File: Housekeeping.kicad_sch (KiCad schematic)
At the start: 117 parts, among them J5 PPS IN, J6 WP Jumper, Q1 FDN335N, Q2 FDN335N, U123 MAX4896, U15 AT24C64D-SSHM, U16 SI5330B-B00206-GM, U19 74AVC4T245, U36 TL071H, U37 TXU0101

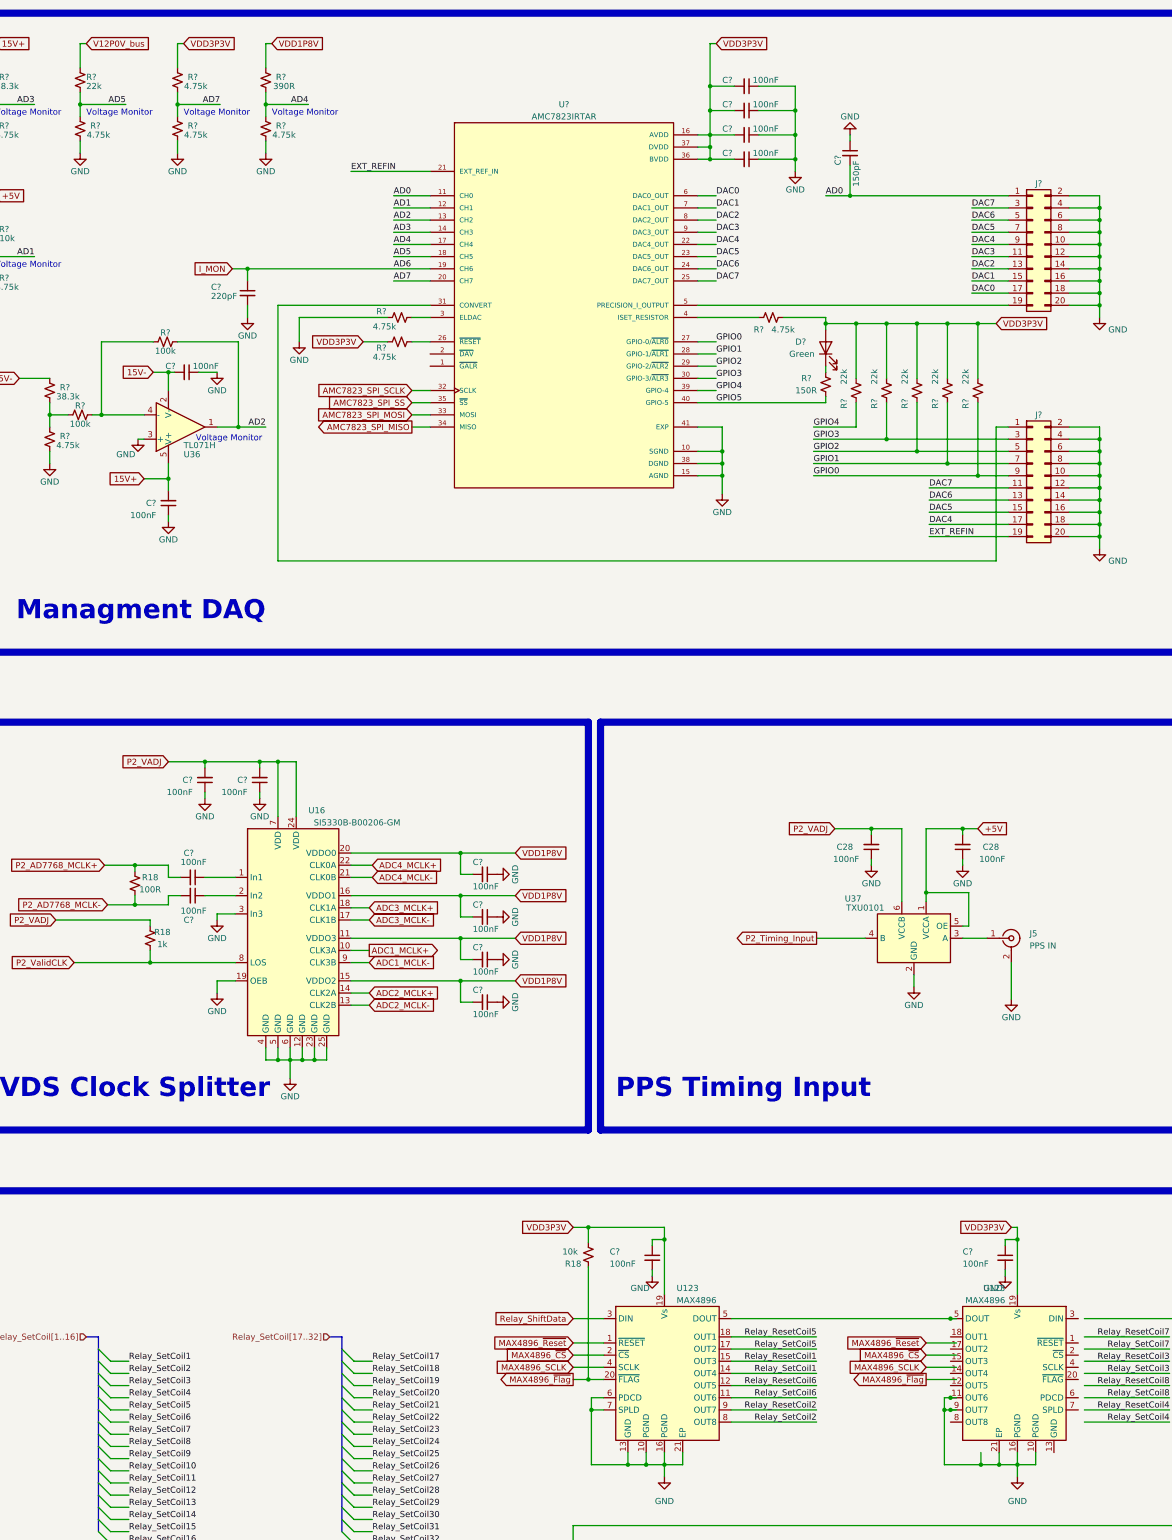
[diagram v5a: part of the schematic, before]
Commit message: Push Version before ADC change from 1.8V to 2.5V I/O
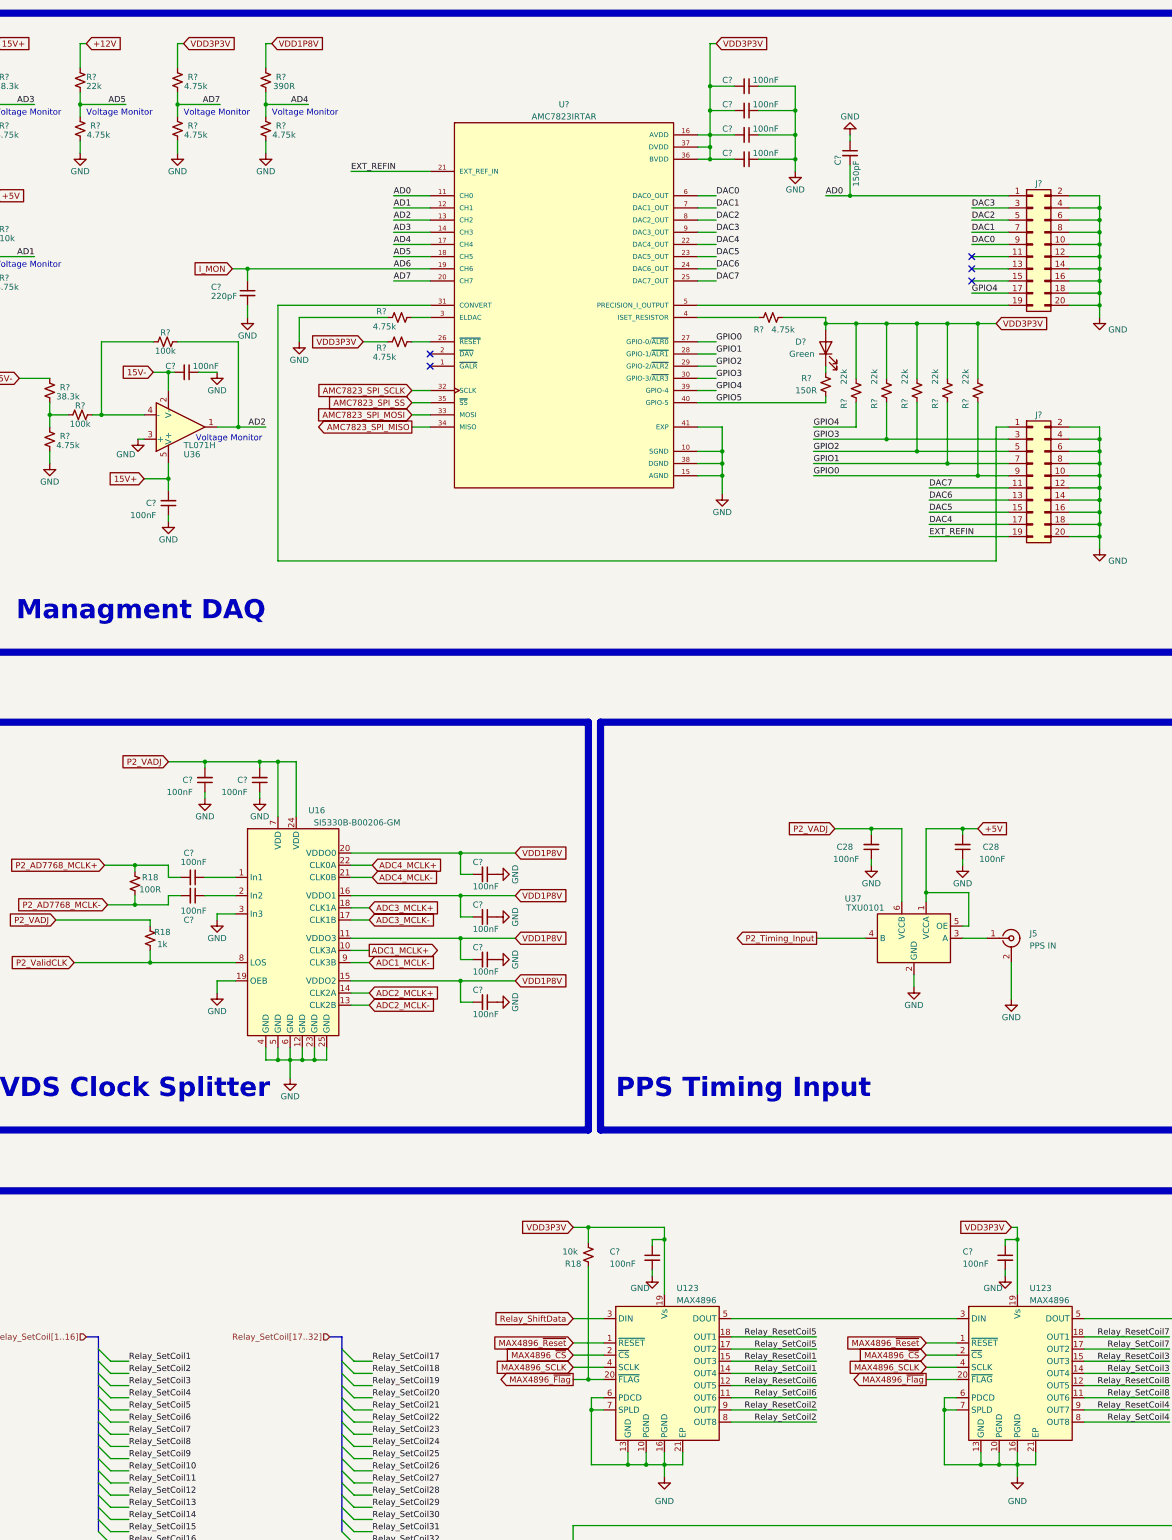
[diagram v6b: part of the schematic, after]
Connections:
- net DAC0: now also J?.9 (Pin_9); no longer J?.17 (Pin_17)
- net DAC1: now also J?.7 (Pin_7); no longer J?.15 (Pin_15)
- net DAC2: now also J?.5 (Pin_5); no longer J?.13 (Pin_13)
- net DAC3: now also J?.3 (Pin_3); no longer J?.11 (Pin_11)
- net DAC4: no longer J?.9 (Pin_9)
- net DAC5: no longer J?.7 (Pin_7)
- net DAC6: no longer J?.5 (Pin_5)
- net DAC7: no longer J?.3 (Pin_3)
- net GND: now also U123.13 (GND), U123.6 (PDCD), U123.7 (SPLD); no longer U123.11 (OUT6), U123.9 (OUT7)
- net GPIO4: now also J?.17 (Pin_17)
- net MAX4896_SCLK: now also U123.4 (SCLK)
- net MAX4896_~{CS}: now also U123.2 (~{CS})
- net MAX4896_~{Flag}: now also U123.20 (~{FLAG})
- net MAX4896_~{Reset}: now also U123.1 (~{RESET})
- net Relay_ResetCoil3: now also U123.15 (OUT3)
- net Relay_ResetCoil4: now also U123.9 (OUT7)
- net Relay_ResetCoil7: now also U123.18 (OUT1)
- net Relay_ResetCoil8: now also U123.12 (OUT5)
- net Relay_SetCoil3: now also U123.14 (OUT4)
- net Relay_SetCoil4: now also U123.8 (OUT8)
- net Relay_SetCoil7: now also U123.17 (OUT2)
- net Relay_SetCoil8: now also U123.11 (OUT6)
- net at U123.5 (DOUT): now also U123.3 (DIN); no longer U123.5 (DOUT)
- net at U123.3 (DIN): now also U123.5 (DOUT)
- net V12P0V_bus renamed +12V
- no-connect marks 1 -> 6
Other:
- moved on the sheet: U123
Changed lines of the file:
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@@
   (junction (at 452.12 154.94) (diameter 0) (color 0 0 0 0)
   )
-  (junction (at 221.615 307.34) (diameter 0) (color 0 0 0 0)
-  )
   (junction (at 252.73 66.675) (diameter 0) (color 0 0 0 0)
   )
-  (junction (at 221.615 288.29) (diameter 0) (color 0 0 0 0)
-  )
   (junction (at 78.74 34.925) (diameter 0) (color 0 0 0 0)
   )
@@
   (junction (at 252.73 74.295) (diameter 0) (color 0 0 0 0)
   )
-  (junction (at 221.615 304.8) (diameter 0) (color 0 0 0 0)
-  )
   (junction (at 408.94 120.015) (diameter 0) (color 0 0 0 0)
   )
@@
   (junction (at 220.98 109.855) (diameter 0) (color 0 0 0 0)
   )
+  (no_connect (at 113.03 89.535))
+  (no_connect (at 226.06 66.675))
+  (no_connect (at 226.06 71.755))
   (no_connect (at 539.75 67.945))
+  (no_connect (at 226.06 69.215))
+  (no_connect (at 113.03 86.995))
   (bus_entry (at 94.615 364.49) (size 2.54 2.54)
     (stroke (width 0) (type default))
@@
     (stroke (width 0) (type default))
   )
-  (wire (pts (xy 226.06 61.595) (xy 233.68 61.595))
-    (stroke (width 0) (type default))
-  )
   (wire (pts (xy 119.38 208.915) (xy 119.38 213.36))
     (stroke (width 0) (type default))
@@
     (stroke (width 0) (type default))
   )
-  (wire (pts (xy 175.895 288.29) (xy 221.615 288.29))
+  (wire (pts (xy 175.895 288.29) (xy 222.885 288.29))
     (stroke (width 0) (type default))
   )
@@
     (stroke (width 0) (type default))
   )
-  (wire (pts (xy 226.06 64.135) (xy 233.68 64.135))
-    (stroke (width 0) (type default))
-  )
   (wire (pts (xy 499.11 88.265) (xy 514.35 88.265))
     (stroke (width 0) (type default))
@@
     (stroke (width 0) (type default))
   )
-  (wire (pts (xy 222.885 307.34) (xy 221.615 307.34))
-    (stroke (width 0) (type default))
-  )
   (wire (pts (xy 227.965 387.35) (xy 231.775 387.35))
     (stroke (width 0) (type default))
@@
     (stroke (width 0) (type default))
   )
+  (bus (pts (xy 43.815 292.1) (xy 43.815 294.64))
+    (stroke (width 0) (type default))
+  )
   (wire (pts (xy 146.05 269.24) (xy 142.875 269.24))
     (stroke (width 0) (type default))
   )
+  (wire (pts (xy 226.06 64.135) (xy 233.68 64.135))
+    (stroke (width 0) (type default))
+  )
   (wire (pts (xy 323.215 370.84) (xy 340.995 370.84))
     (stroke (width 0) (type default))
@@
     (stroke (width 0) (type default))
   )
-  (bus (pts (xy 43.815 292.1) (xy 43.815 294.64))
-    (stroke (width 0) (type default))
-  )
   (wire (pts (xy 515.62 253.365) (xy 515.62 264.795))
     (stroke (width 0) (type default))
@@
     (stroke (width 0) (type default))
   )
-  (wire (pts (xy 222.885 304.8) (xy 221.615 304.8))
-    (stroke (width 0) (type default))
-  )
   (wire (pts (xy 226.06 71.755) (xy 233.68 71.755))
     (stroke (width 0) (type default))
@@
     (stroke (width 0) (type default))
   )
-  (wire (pts (xy 221.615 288.29) (xy 222.885 288.29))
-    (stroke (width 0) (type default))
-  )
   (wire (pts (xy 363.855 300.99) (xy 370.205 300.99))
     (stroke (width 0) (type default))
@@
     (stroke (width 0) (type default))
   )
+  (wire (pts (xy 226.06 61.595) (xy 233.68 61.595))
+    (stroke (width 0) (type default))
+  )
   (wire (pts (xy 46.355 349.25) (xy 50.165 349.25))
     (stroke (width 0) (type default))
@@
     (stroke (width 0) (type default))
   )
-  (wire (pts (xy 221.615 304.8) (xy 220.345 304.8))
+  (wire (pts (xy 220.345 304.8) (xy 222.885 304.8))
     (stroke (width 0) (type default))
   )
@@
     (stroke (width 0) (type default))
   )
+  (wire (pts (xy 226.06 59.055) (xy 233.68 59.055))
+    (stroke (width 0) (type default))
+  )
   (wire (pts (xy 325.755 102.235) (xy 329.565 102.235))
     (stroke (width 0) (type default))
@@
     (stroke (width 0) (type default))
   )
-  (wire (pts (xy 226.06 56.515) (xy 233.68 56.515))
-    (stroke (width 0) (type default))
-  )
   (wire (pts (xy 235.585 337.82) (xy 234.315 337.82))
     (stroke (width 0) (type default))
@@
     (stroke (width 0) (type default))
   )
-  (wire (pts (xy 226.06 59.055) (xy 233.68 59.055))
-    (stroke (width 0) (type default))
-  )
   (bus (pts (xy 43.815 344.17) (xy 43.815 346.71))
     (stroke (width 0) (type default))
@@
     (stroke (width 0) (type default))
   )
+  (wire (pts (xy 226.06 56.515) (xy 233.68 56.515))
+    (stroke (width 0) (type default))
+  )
   (wire (pts (xy 306.705 273.05) (xy 306.705 271.78))
     (stroke (width 0) (type default))
@@
     (stroke (width 0) (type default))
   )
-  (wire (pts (xy 221.615 307.34) (xy 220.345 307.34))
+  (wire (pts (xy 220.345 307.34) (xy 222.885 307.34))
     (stroke (width 0) (type default))
   )
@@
     (effects (font (size 1.27 1.27)) (justify left bottom))
   )
-  (label "DAC1" (at 226.06 71.755 0) (fields_autoplaced)
-    (effects (font (size 1.27 1.27)) (justify left bottom))
-  )
   (label "Relay_SetCoil2" (at 50.165 299.72 0) (fields_autoplaced)
     (effects (font (size 1.27 1.27)) (justify left bottom))
@@
     (effects (font (size 1.27 1.27)) (justify right bottom))
   )
-  (label "Relay_ResetCoil16" (at 50.165 379.73 0) (fields_autoplaced)
+  (label "DAC1" (at 226.06 61.595 0) (fields_autoplaced)
     (effects (font (size 1.27 1.27)) (justify left bottom))
   )
-  (label "DAC3" (at 226.06 66.675 0) (fields_autoplaced)
+  (label "Relay_ResetCoil16" (at 50.165 379.73 0) (fields_autoplaced)
     (effects (font (size 1.27 1.27)) (justify left bottom))
   )
@@
     (effects (font (size 1.27 1.27)) (justify left bottom))
   )
-  (label "DAC4" (at 226.06 64.135 0) (fields_autoplaced)
-    (effects (font (size 1.27 1.27)) (justify left bottom))
-  )
   (label "DAC6" (at 172.72 69.215 0) (fields_autoplaced)
     (effects (font (size 1.27 1.27)) (justify left bottom))
@@
     (effects (font (size 1.27 1.27)) (justify left bottom))
   )
+  (label "DAC3" (at 226.06 56.515 0) (fields_autoplaced)
+    (effects (font (size 1.27 1.27)) (justify left bottom))
+  )
   (label "Relay_ResetCoil10" (at 50.165 364.49 0) (fields_autoplaced)
     (effects (font (size 1.27 1.27)) (justify left bottom))
@@
     (effects (font (size 1.27 1.27)) (justify right bottom))
   )
-  (label "DAC6" (at 226.06 59.055 0) (fields_autoplaced)
-    (effects (font (size 1.27 1.27)) (justify left bottom))
-  )
   (label "Relay_ResetCoil7" (at 267.335 292.1 180) (fields_autoplaced)
     (effects (font (size 1.27 1.27)) (justify right bottom))
@@
     (effects (font (size 1.27 1.27)) (justify right bottom))
   )
-  (label "DAC7" (at 226.06 56.515 0) (fields_autoplaced)
-    (effects (font (size 1.27 1.27)) (justify left bottom))
-  )
   (label "DAC0" (at 172.72 53.975 0) (fields_autoplaced)
     (effects (font (size 1.27 1.27)) (justify left bottom))
@@
     (effects (font (size 1.27 1.27)) (justify left bottom))
   )
-  (label "DAC0" (at 226.06 74.295 0) (fields_autoplaced)
+  (label "DAC0" (at 226.06 64.135 0) (fields_autoplaced)
     (effects (font (size 1.27 1.27)) (justify left bottom))
   )
@@
     (effects (font (size 1.27 1.27)) (justify left bottom))
   )
-  (label "DAC2" (at 226.06 69.215 0) (fields_autoplaced)
-    (effects (font (size 1.27 1.27)) (justify left bottom))
-  )
   (label "AD2" (at 78.74 102.235 180) (fields_autoplaced)
     (effects (font (size 1.27 1.27)) (justify right bottom))
@@
     (effects (font (size 1.27 1.27)) (justify left bottom))
   )
+  (label "DAC2" (at 226.06 59.055 0) (fields_autoplaced)
+    (effects (font (size 1.27 1.27)) (justify left bottom))
+  )
   (label "EXT_REFIN" (at 217.17 125.095 0) (fields_autoplaced)
     (effects (font (size 1.27 1.27)) (justify left bottom))
@@
     (effects (font (size 1.27 1.27)) (justify left bottom))
   )
-  (label "DAC5" (at 226.06 61.595 0) (fields_autoplaced)
-    (effects (font (size 1.27 1.27)) (justify left bottom))
-  )
   (label "Relay_SetCoil4" (at 50.165 304.8 0) (fields_autoplaced)
     (effects (font (size 1.27 1.27)) (justify left bottom))
@@
     (effects (font (size 1.27 1.27)) (justify right bottom))
   )
+  (label "GPIO4" (at 226.06 74.295 0) (fields_autoplaced)
+    (effects (font (size 1.27 1.27)) (justify left bottom))
+  )
   (label "Relay_ResetCoil24" (at 267.335 370.84 180) (fields_autoplaced)
     (effects (font (size 1.27 1.27)) (justify right bottom))
@@
     )
   )
-  (global_label "V12P0V_bus" (shape input) (at 41.275 22.225 0) (fields_autoplaced)
+  (global_label "+12V" (shape input) (at 41.275 22.225 0) (fields_autoplaced)
     (effects (font (size 1.27 1.27)) (justify left))
-    (property "Intersheetrefs" "${INTERSHEET_REFS}" (at 55.5502 22.225 0)
+    (property "Intersheetrefs" "${INTERSHEET_REFS}" (at 49.2608 22.225 0)
       (effects (font (size 1.27 1.27)) (justify left) hide)
     )
@@
     )
   )
-  (symbol (lib_name "MAX4896_1") (lib_id "AD7768_Digitizer_SLib:MAX4896") (at 235.585 297.18 0) (mirror y) (unit 1)
+  (symbol (lib_name "MAX4896_1") (lib_id "AD7768_Digitizer_SLib:MAX4896") (at 235.585 297.18 0) (unit 1)
     (in_bom yes) (on_board yes) (dnp no)
-    (property "Reference" "U123" (at 233.045 281.94 0)
+    (property "Reference" "U123" (at 238.125 281.94 0)
       (effects (font (size 1.27 1.27)) (justify left))
     )
-    (property "Value" "MAX4896" (at 233.045 284.48 0)
+    (property "Value" "MAX4896" (at 238.125 284.48 0)
       (effects (font (size 1.27 1.27)) (justify left))
     )
-    (property "Footprint" "Package_DFN_QFN:TQFN-20-1EP_5x5mm_P0.65mm_EP3.1x3.1mm" (at 247.015 283.21 0)
+    (property "Footprint" "Package_DFN_QFN:TQFN-20-1EP_5x5mm_P0.65mm_EP3.1x3.1mm" (at 224.155 283.21 0)
       (effects (font (size 1.27 1.27)) hide)
     )
-    (property "Datasheet" "" (at 247.015 283.21 0)
+    (property "Datasheet" "" (at 224.155 283.21 0)
       (effects (font (size 1.27 1.27)) hide)
     )

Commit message: Changed ADCs to run on +2.5V VADJ
Modified schematic to allow the ADCs to be run from the +2.5V VADJ inputs on the FMC connector.
-All relevant ERC issues ran been looked into.
-Still working on all Board DRC issues.
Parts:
- removed C? (x8): 100nF, Capacitor_SMD:C_0402_1005Metric, symbol Device:C_Small
- removed C?: 150pF, Capacitor_SMD:C_0402_1005Metric, symbol Device:C_Small
- removed R? (x3): 4.75k, Resistor_SMD:R_0402_1005Metric, symbol Device:R_Small_US
- removed R? (x4): 10k, Resistor_SMD:R_0402_1005Metric, symbol Device:R_Small_US
- removed R?: 390R, Resistor_SMD:R_0603_1608Metric, symbol Device:R_Small_US
- removed R?: 4.75k, Resistor_SMD:R_0603_1608Metric, symbol Device:R_Small_US
- removed U19 (x3): 74AVC4T245, Package_SO:TSSOP-16_4.4x5mm_P0.65mm, symbol Custom_Lib_MPEX_Zest:74LVC4T245
- removed U?: 74LVC8T245, Package_SO:TSSOP-24_4.4x7.8mm_P0.65mm, symbol Custom_Lib_MPEX_Zest:74LVC8T245
- added C? (x2): 150pF, Capacitor_SMD:C_0402_1005Metric, symbol Device:C_Small
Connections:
- net AD0: now also C?.2
- net AD4: now also J?.3 (Pin_3), C?.2
- net DAC0: now also J?.11 (Pin_11); no longer J?.9 (Pin_9)
- net DAC1: now also J?.9 (Pin_9); no longer J?.7 (Pin_7)
- net DAC2: now also J?.7 (Pin_7); no longer J?.5 (Pin_5)
- net DAC3: now also J?.5 (Pin_5); no longer J?.3 (Pin_3)
- net GND: now also C?.1, C?.1
- net P1_VADJ: now also C?.2, C?.2, U16.11 (VDDO3), U16.15 (VDDO2)
- net P2_VADJ: now also C?.2, C?.2, U16.16 (VDDO1), U16.20 (VDDO0)
- removed net VDD1P8V: C?.2, C?.2, C?.2, C?.2, U16.11 (VDDO3), U16.15 (VDDO2), U16.16 (VDDO1), U16.20 (VDDO0)
- no-connect marks 6 -> 5
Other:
- moved on the sheet: C28, R?, U19

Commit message: Completed Schmatic and Layout
All Schematic and Layout Task are complete with the following exceptions:
- Adjust Silkscreen Layers
- Add Osprey Logo and Serial Number

Note-Removed Files no longer reference in the project
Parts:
- removed C? (x2): 150pF, Capacitor_SMD:C_0402_1005Metric, symbol Device:C_Small
- removed C?: 220pF, Capacitor_SMD:C_0402_1005Metric, symbol Device:C_Small
- removed J?: Conn_02x10_Odd_Even, Connector_PinHeader_1.27mm:PinHeader_2x10_P1.27mm_Vertical_SMD, symbol Connector_Generic:Conn_02x10_Odd_Even
- removed R18: 1k, Resistor_SMD:R_0402_1005Metric, symbol Device:R_Small_US
- removed R?: 22k, Resistor_SMD:R_0402_1005Metric, symbol Device:R_Small_US
- added R? (x2): 4.75k, Resistor_SMD:R_0603_1608Metric, symbol Device:R_Small_US
- added R? (x2): 2.49k, Resistor_SMD:R_0603_1608Metric, symbol Device:R_Small_US
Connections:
- net AD0: now also R?.2, U36.1
- net AD1: now also R?.1, R?.2; no longer R?.1, R?.2
- net AD2: now also R?.1, R?.2; no longer R?.2, U36.1
- net AD3: now also R?.1, R?.2; no longer R?.1, R?.2
- net AD4: now also R?.1, R?.2
- net AD5: now also R?.1, R?.2; no longer R?.1, R?.2
- net GND: now also R?.2, R?.2
- net I_MON: now also U?.20 (CH7); no longer U?.19 (CH6)
- net P2_VADJ: no longer C28.2, C28.2, C?.2, C?.2, C?.2, C?.2, C?.2, R?.2, U16.16 (VDDO1), U16.20 (VDDO0), U16.24 (VDD), U16.7 (VDD), U19.1 (VCCA), U37.6 (VCCB), U?.1 (VCCA)
- removed net AD7: R?.1, R?.2, U?.20 (CH7)
- net GPIO4: no longer names the net of U?.39 (GPIO-4)
- net P1_VADJ renamed P1_2P5V
- net P1_2P5V: now also R?.1
- new net AD6: R?.1, R?.2, U?.19 (CH6)
- new net P2_2P5V: C28.2, C28.2, C?.2, C?.2, C?.2, C?.2, C?.2, R?.1, R?.2, U16.16 (VDDO1), U16.20 (VDDO0), U16.24 (VDD), U16.7 (VDD), U19.1 (VCCA), U37.6 (VCCB), U?.1 (VCCA)
- no-connect marks 5 -> 9
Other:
- note added: "Management DAQ"
- note removed: "From ADCs"
- note removed: "Managment DAQ"
- note removed: "To ADCs"
- moved on the sheet: C28, C?, D3, D?, H1, H2, J5, J6, J?, Q1, Q2, R18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
